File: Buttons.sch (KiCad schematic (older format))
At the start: 11 parts, among them SW3 sw_vol, SW4 Rotary_Encoder, SW5 sw_fadein, SW6 sw_fadeout, SW7 sw_touch, SW8 sw_mode, SW9 sw_release, U5 TCA9534

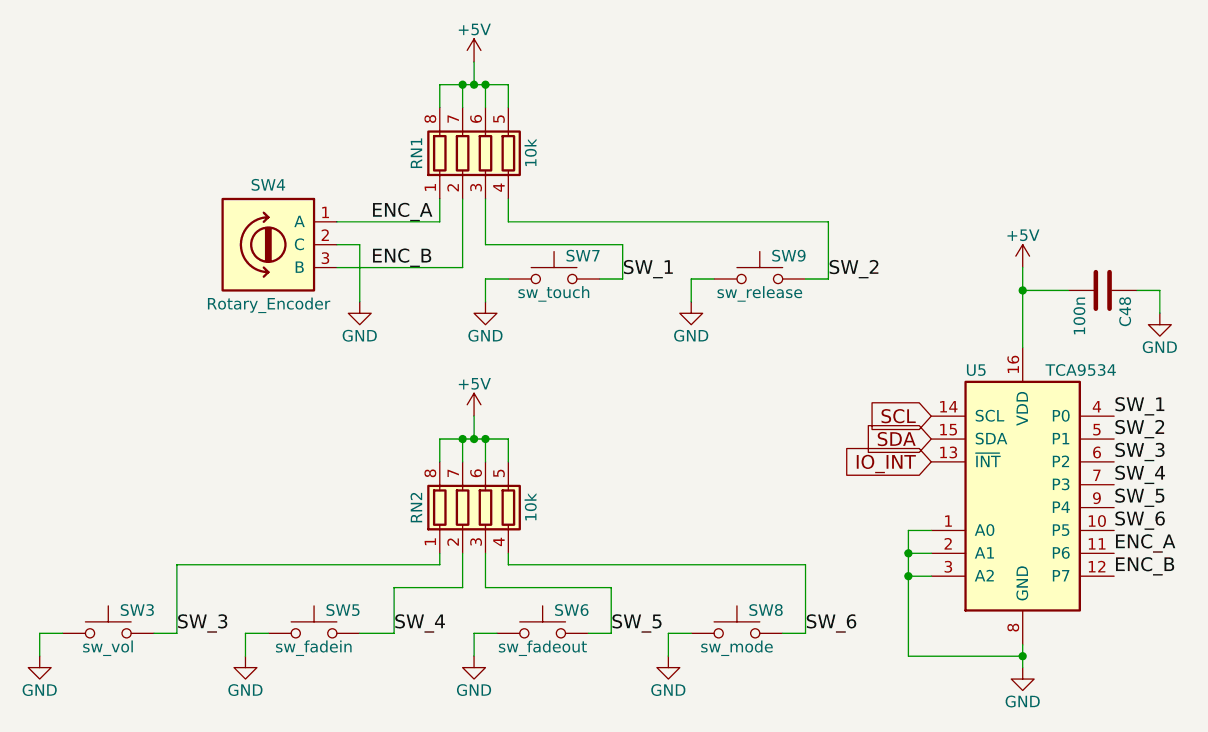
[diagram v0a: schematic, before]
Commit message: Board should be ok. Bargraph leds yet to do.
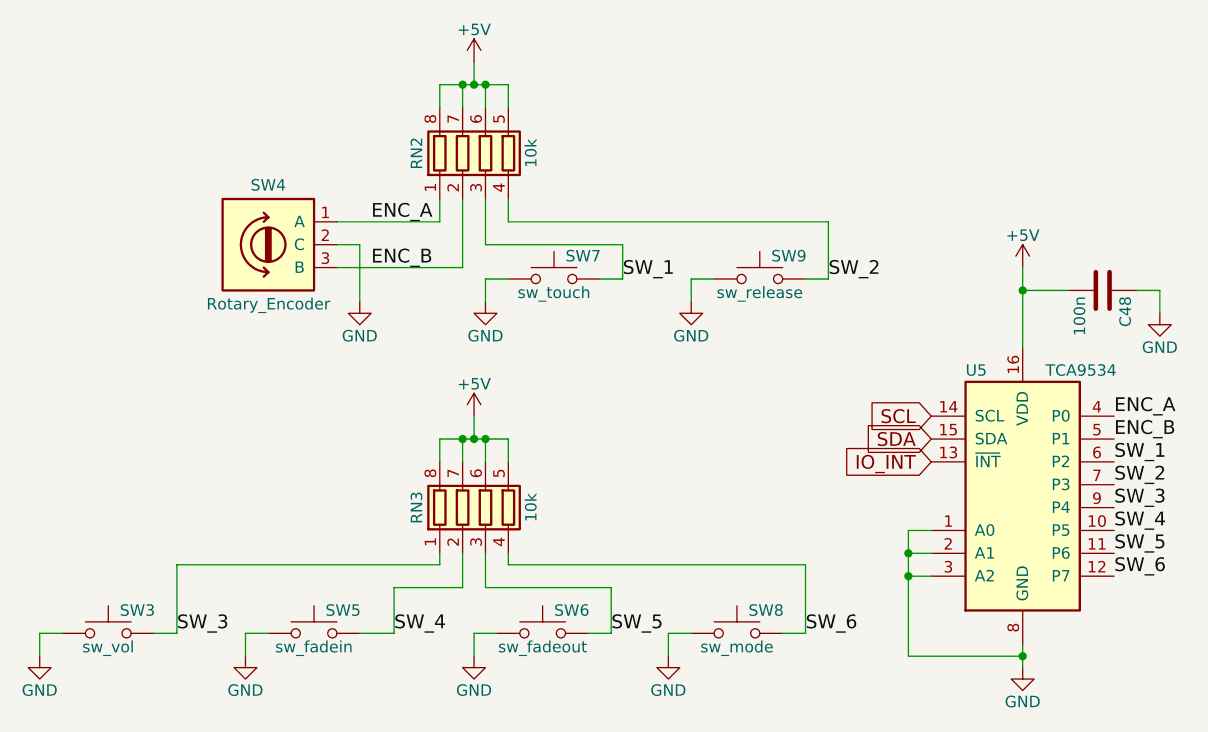
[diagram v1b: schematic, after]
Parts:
- renumbered RN1 to RN2, RN2 to RN3
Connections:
- net ENC_A: now also U5.4 (P0); no longer U5.11 (P6)
- net ENC_B: now also U5.5 (P1); no longer U5.12 (P7)
- net SW_1: now also U5.6 (P2); no longer U5.4 (P0)
- net SW_2: now also U5.7 (P3); no longer U5.5 (P1)
- net SW_3: now also U5.9 (P4); no longer U5.6 (P2)
- net SW_4: now also U5.10 (P5); no longer U5.7 (P3)
- net SW_5: now also U5.11 (P6); no longer U5.9 (P4)
- net SW_6: now also U5.12 (P7); no longer U5.10 (P5)
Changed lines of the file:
@@
 SW_5
 $Comp
-L R_Pack04 RN1
+L R_Pack04 RN2
 U 1 1 59B017A5
 P 4450 2200
-F 0 "RN1" V 4150 2200 50  0000 C CNN
+F 0 "RN2" V 4150 2200 50  0000 C CNN
 F 1 "10k" V 4650 2200 50  0000 C CNN
 F 2 "Resistors_SMD:R_Array_Concave_4x0603" V 4725 2200 50  0001 C CNN
@@
 Connection ~ 4400 1900
 $Comp
-L R_Pack04 RN2
+L R_Pack04 RN3
 U 1 1 59B01A70
 P 4450 3750
-F 0 "RN2" V 4150 3750 50  0000 C CNN
+F 0 "RN3" V 4150 3750 50  0000 C CNN
 F 1 "10k" V 4650 3750 50  0000 C CNN
 F 2 "Resistors_SMD:R_Array_Concave_4x0603" V 4725 3750 50  0001 C CNN
@@
 Text GLabel 6400 3350 0    60   Input ~ 0
 SCL
+Text Label 7200 3550 0    60   ~ 0
+SW_1
+Text Label 7200 3650 0    60   ~ 0
+SW_2
+Text Label 7200 3750 0    60   ~ 0
+SW_3
+Text Label 7200 3850 0    60   ~ 0
+SW_4
+Text Label 7200 3950 0    60   ~ 0
+SW_5
+Text Label 7200 4050 0    60   ~ 0
+SW_6
 Text Label 7200 3350 0    60   ~ 0
-SW_1
+ENC_A
 Text Label 7200 3450 0    60   ~ 0
-SW_2
-Text Label 7200 3550 0    60   ~ 0
-SW_3
-Text Label 7200 3650 0    60   ~ 0
-SW_4
-Text Label 7200 3750 0    60   ~ 0
-SW_5
-Text Label 7200 3850 0    60   ~ 0
-SW_6
-Text Label 7200 3950 0    60   ~ 0
-ENC_A
-Text Label 7200 4050 0    60   ~ 0
 ENC_B
 $Comp

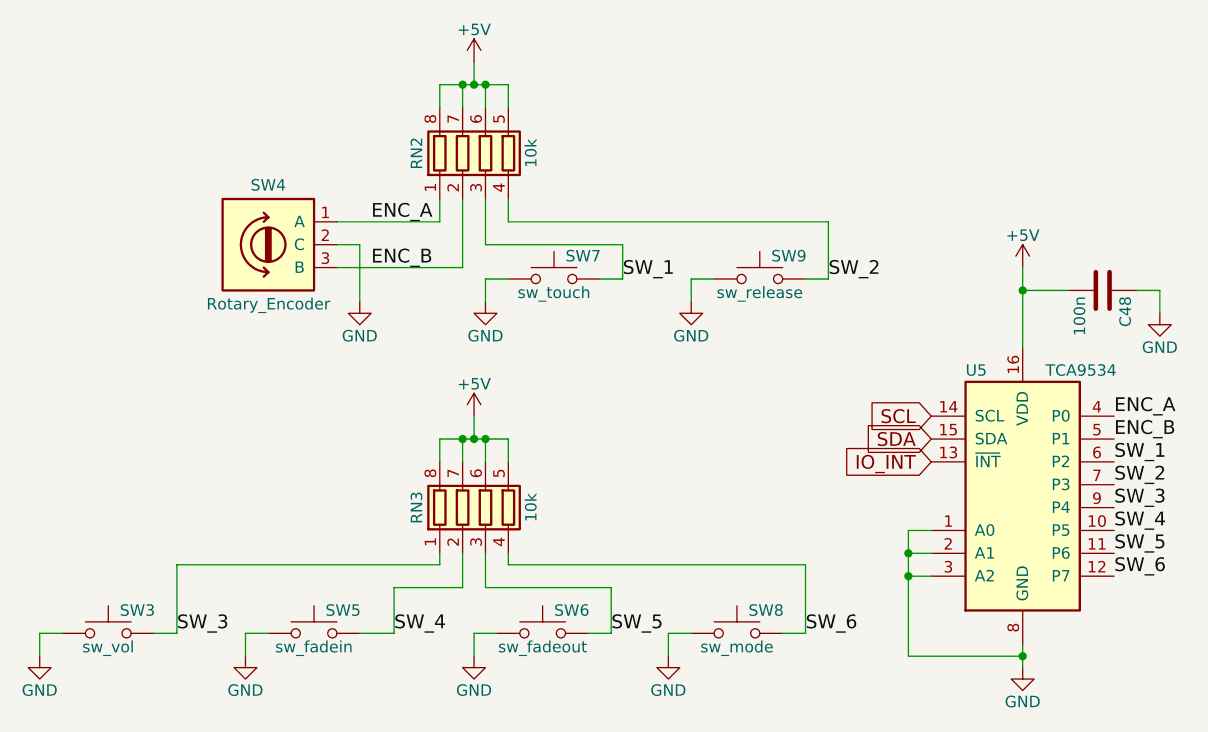
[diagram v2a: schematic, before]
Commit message: Board modified after ckecking. Ready for fab, just need to create gerber, position and components files.
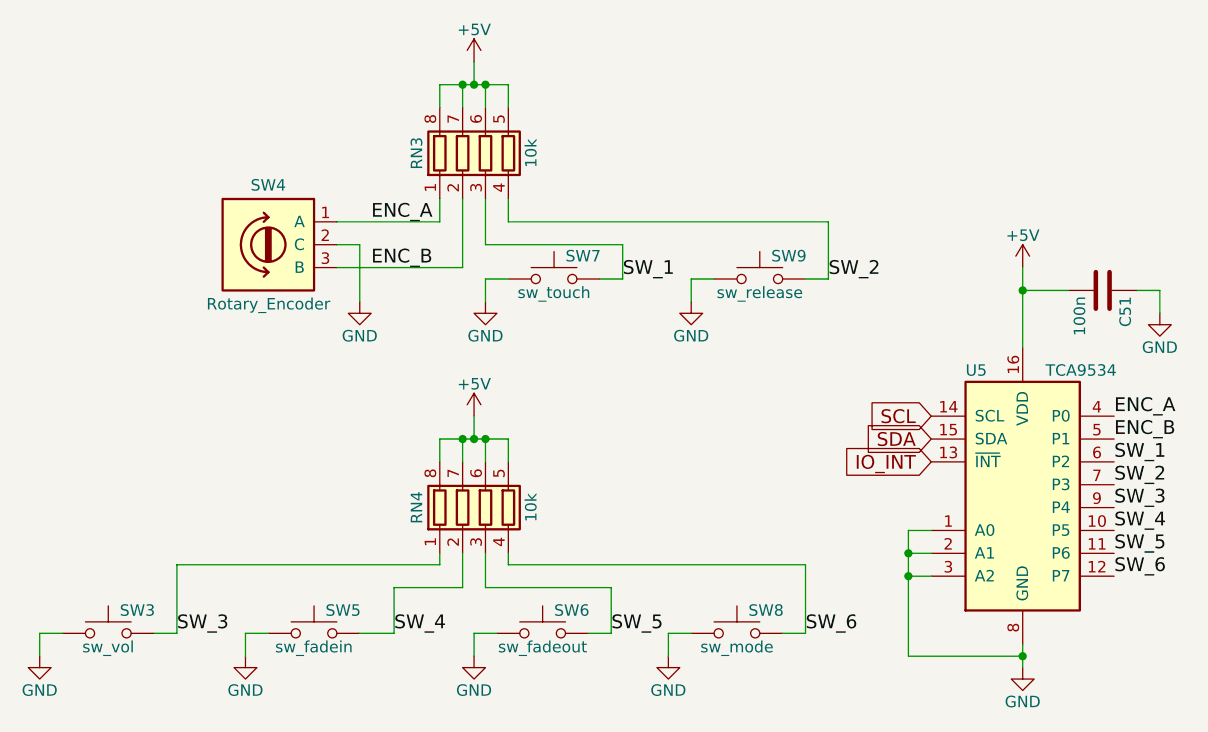
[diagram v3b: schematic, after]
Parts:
- renumbered C48 to C51, RN2 to RN3, RN3 to RN4
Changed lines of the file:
@@
 EESchema Schematic File Version 2
+LIBS:ContactConsequencesMono-rescue
 LIBS:switches-perso
 LIBS:Logos
@@
 $EndComp
 $Comp
-L GND #PWR063
+L GND #PWR071
 U 1 1 59B00F71
 P 4450 2850
-F 0 "#PWR063" H 4450 2600 50  0001 C CNN
+F 0 "#PWR071" H 4450 2600 50  0001 C CNN
 F 1 "GND" H 4450 2700 50  0000 C CNN
 F 2 "" H 4450 2850 50  0001 C CNN
@@
 $EndComp
 $Comp
-L GND #PWR064
+L GND #PWR072
 U 1 1 59B012C1
 P 5350 2850
-F 0 "#PWR064" H 5350 2600 50  0001 C CNN
+F 0 "#PWR072" H 5350 2600 50  0001 C CNN
 F 1 "GND" H 5350 2700 50  0000 C CNN
 F 2 "" H 5350 2850 50  0001 C CNN
@@
 $EndComp
 $Comp
-L GND #PWR065
+L GND #PWR073
 U 1 1 59B0148B
 P 2500 4400
-F 0 "#PWR065" H 2500 4150 50  0001 C CNN
+F 0 "#PWR073" H 2500 4150 50  0001 C CNN
 F 1 "GND" H 2500 4250 50  0000 C CNN
 F 2 "" H 2500 4400 50  0001 C CNN
@@
 $EndComp
 $Comp
-L GND #PWR066
+L GND #PWR074
 U 1 1 59B0149B
 P 3400 4400
-F 0 "#PWR066" H 3400 4150 50  0001 C CNN
+F 0 "#PWR074" H 3400 4150 50  0001 C CNN
 F 1 "GND" H 3400 4250 50  0000 C CNN
 F 2 "" H 3400 4400 50  0001 C CNN
@@
 $EndComp
 $Comp
-L GND #PWR067
+L GND #PWR075
 U 1 1 59B0166D
 P 4400 4400
-F 0 "#PWR067" H 4400 4150 50  0001 C CNN
+F 0 "#PWR075" H 4400 4150 50  0001 C CNN
 F 1 "GND" H 4400 4250 50  0000 C CNN
 F 2 "" H 4400 4400 50  0001 C CNN
@@
 SW_5
 $Comp
-L R_Pack04 RN2
+L R_Pack04 RN3
 U 1 1 59B017A5
 P 4450 2200
-F 0 "RN2" V 4150 2200 50  0000 C CNN
+F 0 "RN3" V 4150 2200 50  0000 C CNN
 F 1 "10k" V 4650 2200 50  0000 C CNN
 F 2 "Resistors_SMD:R_Array_Concave_4x0603" V 4725 2200 50  0001 C CNN
@@
 $EndComp
 $Comp
-L +5V #PWR068
+L +5V #PWR076
 U 1 1 59B01820
 P 4400 1800
-F 0 "#PWR068" H 4400 1650 50  0001 C CNN
+F 0 "#PWR076" H 4400 1650 50  0001 C CNN
 F 1 "+5V" H 4400 1940 50  0000 C CNN
 F 2 "" H 4400 1800 50  0001 C CNN
@@
 Connection ~ 4400 1900
 $Comp
-L R_Pack04 RN3
+L R_Pack04 RN4
 U 1 1 59B01A70
 P 4450 3750
-F 0 "RN3" V 4150 3750 50  0000 C CNN
+F 0 "RN4" V 4150 3750 50  0000 C CNN
 F 1 "10k" V 4650 3750 50  0000 C CNN
 F 2 "Resistors_SMD:R_Array_Concave_4x0603" V 4725 3750 50  0001 C CNN
@@
 $EndComp
 $Comp
-L +5V #PWR069
+L +5V #PWR077
 U 1 1 59B01C1D
 P 4400 3350
-F 0 "#PWR069" H 4400 3200 50  0001 C CNN
+F 0 "#PWR077" H 4400 3200 50  0001 C CNN
 F 1 "+5V" H 4400 3490 50  0000 C CNN
 F 2 "" H 4400 3350 50  0001 C CNN
@@
 $EndComp
 $Comp
-L +5V #PWR070
+L +5V #PWR078
 U 1 1 59B033D0
 P 6800 2700
-F 0 "#PWR070" H 6800 2550 50  0001 C CNN
+F 0 "#PWR078" H 6800 2550 50  0001 C CNN
 F 1 "+5V" H 6800 2840 50  0000 C CNN
 F 2 "" H 6800 2700 50  0001 C CNN
@@
 	6800 2700 6800 3050
 $Comp
-L GND #PWR071
+L GND #PWR079
 U 1 1 59B03444
 P 6800 4450
-F 0 "#PWR071" H 6800 4200 50  0001 C CNN
+F 0 "#PWR079" H 6800 4200 50  0001 C CNN
 F 1 "GND" H 6800 4300 50  0000 C CNN
 F 2 "" H 6800 4450 50  0001 C CNN
@@
 ENC_B
 $Comp
-L C C48
+L C C51
 U 1 1 59B1EB45
 P 7150 2800
-F 0 "C48" H 7175 2900 50  0000 L CNN
+F 0 "C51" H 7175 2900 50  0000 L CNN
 F 1 "100n" H 7175 2700 50  0000 L CNN
 F 2 "Capacitors_SMD:C_0603" H 7188 2650 50  0001 C CNN
@@
 	6800 2800 7000 2800
 $Comp
-L GND #PWR072
+L GND #PWR080
 U 1 1 59B1EC53
 P 7400 2900
-F 0 "#PWR072" H 7400 2650 50  0001 C CNN
+F 0 "#PWR080" H 7400 2650 50  0001 C CNN
 F 1 "GND" H 7400 2750 50  0000 C CNN
 F 2 "" H 7400 2900 50  0001 C CNN
@@
 $EndComp
 $Comp
-L GND #PWR073
+L GND #PWR081
 U 1 1 59C81CAC
 P 5250 4400
-F 0 "#PWR073" H 5250 4150 50  0001 C CNN
+F 0 "#PWR081" H 5250 4150 50  0001 C CNN
 F 1 "GND" H 5250 4250 50  0000 C CNN
 F 2 "" H 5250 4400 50  0001 C CNN
@@
 	4350 2700 3800 2700
 $Comp
-L GND #PWR074
+L GND #PWR082
 U 1 1 59C94163
 P 3900 2850
-F 0 "#PWR074" H 3900 2600 50  0001 C CNN
+F 0 "#PWR082" H 3900 2600 50  0001 C CNN
 F 1 "GND" H 3900 2700 50  0000 C CNN
 F 2 "" H 3900 2850 50  0001 C CNN

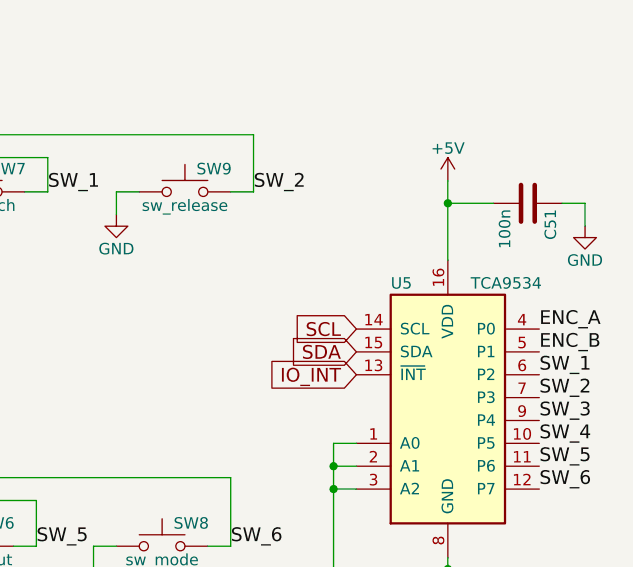
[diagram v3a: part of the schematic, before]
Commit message: v0.2 ready for fabrication. Voltage regulators replaced by cheaper ones.
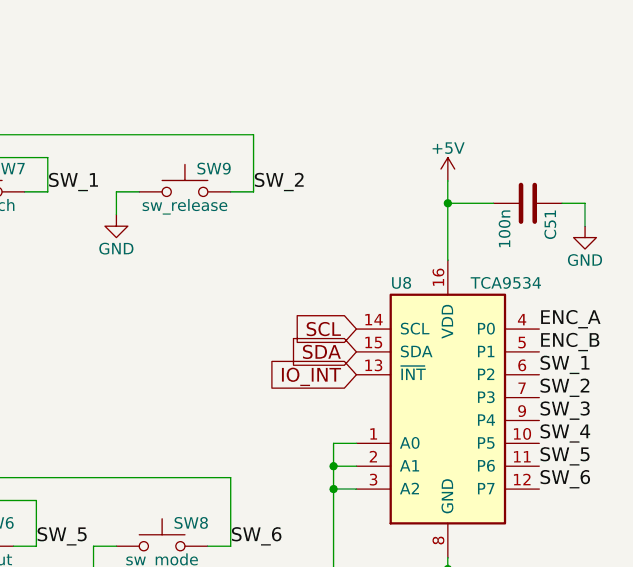
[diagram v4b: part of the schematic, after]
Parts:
- renumbered U5 to U8
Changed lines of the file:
@@
 Connection ~ 4400 3450
 $Comp
-L TCA9534 U5
+L TCA9534 U8
 U 1 1 59B0316F
 P 6800 3650
-F 0 "U5" H 6550 4150 50  0000 L CNN
+F 0 "U8" H 6550 4150 50  0000 L CNN
 F 1 "TCA9534" H 6900 4150 50  0000 L CNN
 F 2 "Housings_SSOP:TSSOP-16_4.4x5mm_Pitch0.65mm" H 7750 3100 50  0001 C CNN
